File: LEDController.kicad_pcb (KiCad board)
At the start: 2 copper layers, 13 parts, among them J1 3557-2, J10 3557-2, J16 3557-2, J2 3557-2, J3 3557-2, J4 3557-2, J5 3557-2, J6 3557-2, J7 3557-2, J8 3557-2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

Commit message: updated pcb
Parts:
- added D2: S1M, SamacSys_Parts:DIOM5336X240N, F.Cu at (84.0, 52.3)
- added J11: TB002-500-04BE, SamacSys_Parts:CONN4_TB002-500_787x299_CUD, F.Cu at (75.5, 54.5)
- added J12: TB002-500-04BE, SamacSys_Parts:CONN4_TB002-500_787x299_CUD, F.Cu at (75.5, 63.7)
- added J17: TB002-500-04BE, SamacSys_Parts:CONN4_TB002-500_787x299_CUD, F.Cu at (75.5, 73.0)
- added R1: 1K, Resistor_SMD:R_0603_1608Metric_Pad0.98x0.95mm_HandSolder, F.Cu at (82.1, 56.3)
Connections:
- J1 pad 2: Net-(K1-COM) -> Net-(D2-A)
- J1 pad 4: Net-(K1-COM) -> Net-(D2-A)
- J2 pad 2: Net-(K1-COM) -> Net-(D2-A)
- J2 pad 4: Net-(K1-COM) -> Net-(D2-A)
- J3 pad 2: Net-(K1-COM) -> Net-(D2-A)
- J3 pad 4: Net-(K1-COM) -> Net-(D2-A)
- J4 pad 2: Net-(K1-COM) -> Net-(D2-A)
- J4 pad 4: Net-(K1-COM) -> Net-(D2-A)
- J5 pad 2: Net-(K1-COM) -> Net-(D2-A)
- J5 pad 4: Net-(K1-COM) -> Net-(D2-A)
- J6 pad 2: Net-(K1-COM) -> Net-(D2-A)
- J6 pad 4: Net-(K1-COM) -> Net-(D2-A)
- K1 pad 2: unconnected-(K1-COIL_2-Pad2) -> Net-(D2-A)
- K1 pad 3: Net-(K1-COM) -> Net-(D2-A)
- Q1 pad 1: unconnected-(Q1-E-Pad1) -> GND
- Q1 pad 2: unconnected-(Q1-C_1-Pad2) -> Net-(D2-A)
- Q1 pad 3: unconnected-(Q1-B-Pad3) -> Net-(Q1-B)
- Q1 pad 4: unconnected-(Q1-C_2-Pad4) -> Net-(D2-A)

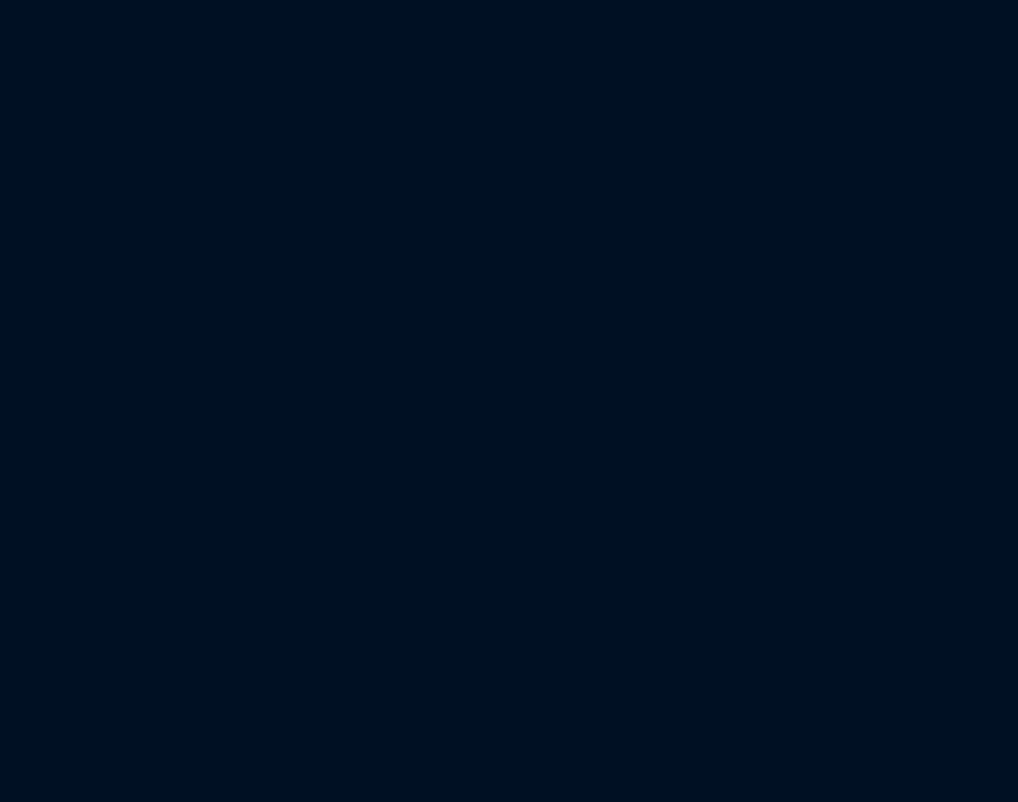
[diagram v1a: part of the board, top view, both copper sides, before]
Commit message: Added new high current terminal
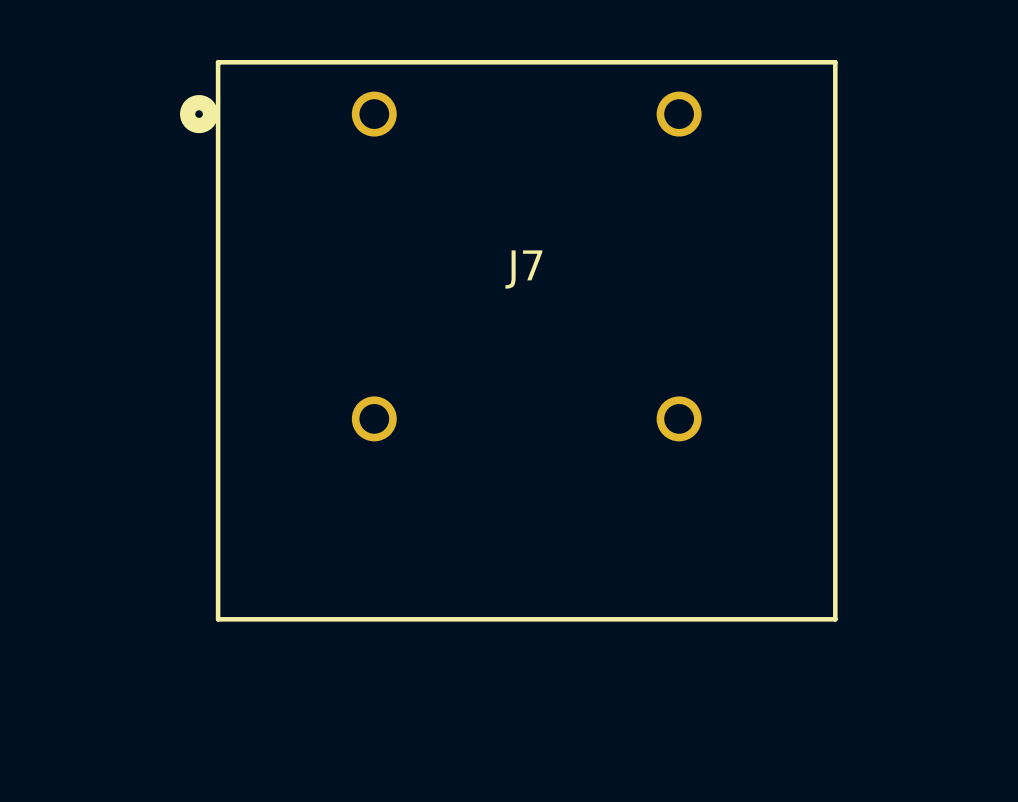
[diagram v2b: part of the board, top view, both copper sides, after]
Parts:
- added J7: VP0265840000G, SamacSys_Parts:CONN04_VP026584_20P32X18P3_AMP, F.Cu at (183.8, 18.3)
